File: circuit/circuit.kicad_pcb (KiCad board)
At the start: 2 copper layers, 19 parts

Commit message: circuit building
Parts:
- added BATT1: M02PTH, SparkFun:SparkFun-1X02_XTRA_BIG, F.Cu at (133.1, 81.8)
- added BATT2: M02PTH, SparkFun:SparkFun-1X02_XTRA_BIG, F.Cu at (133.1, 92.7)
- added BATT3: M02PTH, SparkFun:SparkFun-1X02_XTRA_BIG, F.Cu at (133.2, 103.3)
- added BATT4: M02PTH, SparkFun:SparkFun-1X02_XTRA_BIG, F.Cu at (133.2, 114.3)
- added C-ADC1: 100n, Capacitors_SMD:C_0805_HandSoldering, F.Cu at (140.4, 84.2)
- added CON-PV1: BARREL_JACK, Connect:JACK_ALIM, B.Cu at (165.8, 93.7)
- added C_VUSB1: 100u, Capacitors_ThroughHole:C_Radial_D5_L6_P2.5, B.Cu at (135.1, 135.2)
- added C_VUSB2: 100u, Capacitors_ThroughHole:C_Radial_D5_L6_P2.5, B.Cu at (135.1, 142.0)
- added D-3V3: D, Diodes_SMD:SMA_Handsoldering, F.Cu at (150.4, 95.5)
- added D-LAMP1: D, Diodes_SMD:SMA_Handsoldering, F.Cu at (172.0, 122.7)
- added D-PV1: D, Diodes_SMD:SMA_Handsoldering, F.Cu at (171.7, 108.1)
- added D-USB1: D, Diodes_SMD:SMA_Handsoldering, F.Cu at (146.9, 131.3)
- added D-VDD1: D, Diodes_SMD:SMA_Handsoldering, F.Cu at (138.9, 103.9)
- added D-VUSB1: D_Schottky, Diodes_SMD:SMA_Handsoldering, F.Cu at (135.9, 131.3)
- added D-VUSB2: D_Schottky, Diodes_SMD:SMA_Handsoldering, F.Cu at (129.3, 149.1)
- added D1: 5v1, Diodes_SMD:MELF_Handsoldering, F.Cu at (138.5, 149.1)
- added IC-VUSB1: LM2596S, TO_SOT_Packages_SMD:TO-263-5Lead, F.Cu at (147.6, 140.0)
- added L-VUSB1: INDUCTOR, Inductors:INDUCTOR_V, B.Cu at (141.2, 139.7)
- added OK-LAMP1: PC817, Housings_DIP:DIP-4_W7.62mm, B.Cu at (156.3, 124.0)
- added OK-PV1: PC817, Housings_DIP:DIP-4_W7.62mm, B.Cu at (155.9, 84.9)
- added OK-PV2: PC817, Housings_DIP:DIP-4_W7.62mm, B.Cu at (155.9, 110.4)
- added OK-USB1: PC817, Housings_DIP:DIP-4_W7.62mm, B.Cu at (146.3, 115.6)
- added P-VDD-3V3: CONN_01X02, Pin_Headers:Pin_Header_Straight_1x02, B.Cu at (140.7, 95.5)
- added P1: USB_A, Connect:USB_A, B.Cu at (140.5, 153.2)
- added R-ADC-BATT1: 470k, Resistors_ThroughHole:Resistor_Horizontal_RM10mm, B.Cu at (137.3, 84.2)
- added R-ADC-BATT2: 100k, Resistors_ThroughHole:Resistor_Horizontal_RM10mm, B.Cu at (140.4, 84.2)
- added R-LAMP1: 330, Resistors_SMD:R_0805_HandSoldering, F.Cu at (159.5, 123.7)
- added R-LAMP2: 4k7, Resistors_SMD:R_0805_HandSoldering, F.Cu at (165.4, 117.9)
- added R-PV1: 4k7, Resistors_SMD:R_0805_HandSoldering, F.Cu at (152.2, 89.0)
- added R-PV2: 100k, Resistors_SMD:R_0805_HandSoldering, F.Cu at (158.8, 88.3)
- added R-PV3: 330, Resistors_SMD:R_0805_HandSoldering, F.Cu at (159.7, 113.4)
- added R-PV4: 4k7, Resistors_SMD:R_0805_HandSoldering, F.Cu at (161.6, 103.8)
- added R-USB1: 330, Resistors_SMD:R_0805_HandSoldering, F.Cu at (148.2, 118.1)
- added R-USB2: 4k7, Resistors_SMD:R_0805_HandSoldering, F.Cu at (151.9, 122.8)
- added SW-PWR1: CONN_01X02, Pin_Headers:Pin_Header_Straight_1x02, B.Cu at (128.6, 118.4)
- added TR-LAMP1: IRF530_TO220BV, transistor-power:TO220BV, B.Cu at (165.4, 123.2)
- added TR-PV1: IRF9530_TO220BV, transistor-power:TO220BV, B.Cu at (164.7, 108.2)
- added TR-USB1: IRF530_TO220BV, transistor-power:TO220BV, B.Cu at (146.1, 124.5)
- added U1: MIC5219BM5_SOT23-5, TO_SOT_Packages_SMD:SOT-23-5, F.Cu at (145.1, 101.9)
- L-LAMP1, L-PV1, L-USB1, L1, L2, L3, L4: footprint LEDs:LED-1206 -> LEDs:LED-0805
- P-BOOT1, P-COMM1, SW-NRST1: moved to B.Cu
- R-L-LAMP1, R-L-PV1, R-L-USB1, R-L1, R-L2, R-L3, R-L4, R-NRST1: footprint Resistors_SMD:R_1206_HandSoldering -> Resistors_SMD:R_0805_HandSoldering
- moved STM32 31.7 mm to (152.6, 72.4)
- moved SW-NRST1 31.5 mm to (138.9, 68.2), turned to 90 degrees
- moved R-NRST1 31.0 mm to (143.7, 68.3)
- moved P-COMM1 30.9 mm to (167.8, 65.9), turned to 180 degrees
- moved R-L2 30.6 mm to (152.2, 57.7)
- moved R-L-PV1 30.6 mm to (163.0, 57.8)
- moved R-L4 30.6 mm to (157.7, 57.7)
- moved R-L-LAMP1 30.6 mm to (143.4, 57.3)
- moved R-L-USB1 30.6 mm to (140.7, 57.3)
- moved R-L1 30.6 mm to (149.4, 57.7)
- moved R-L3 30.6 mm to (155.0, 57.7)
- moved L1 29.2 mm to (149.3, 52.7)
- moved L-LAMP1 29.2 mm to (143.2, 52.5)
- moved L-PV1 29.2 mm to (162.6, 52.6)
- moved L-USB1 29.2 mm to (140.4, 52.5)
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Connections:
- P-COMM1 pad 3: /TX -> /RX
- P-COMM1 pad 4: /RX -> /TX
- STM32 pad 10: /ADC_PV_WKUP -> /IND_PV_WKUP
- STM32 pad 25: Net-(STM32-Pad25) -> /CON_PV
- STM32 pad 26: Net-(STM32-Pad26) -> /CON_LAMP
- STM32 pad 27: Net-(STM32-Pad27) -> /CON_USB
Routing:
- net GND: track 0.00 -> 39.6 mm
- net /ADC_BATT: track 0.00 -> 24.7 mm, vias 0 -> 2
- net /IND_PV_WKUP: track 0.00 -> 23.8 mm
- net /BOOT0: track 0.00 -> 23.3 mm
- net /L-USB: track 0.00 -> 16.0 mm
- net /L-PV: track 0.00 -> 15.5 mm
- net /L-LAMP: track 0.00 -> 14.0 mm
- net GNDPWR: track 0.00 -> 12.5 mm
- net /TX: track 0.00 -> 11.4 mm
- net /RX: track 0.00 -> 11.3 mm
- net /L-L4: track 0.00 -> 10.9 mm
- net /L-L1: track 0.00 -> 10.2 mm
- net /NRST: track 0.00 -> 9.08 mm
- net Net-(OK-PV2-Pad3): track 0.00 -> 9.07 mm
- net /L-L3: track 0.00 -> 9.05 mm
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
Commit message: development
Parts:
- added L-IND1: LED, LEDs:LED-0805, F.Cu at (166.6, 52.6)
- added R-L-IND1: 330, Resistors_SMD:R_0805_HandSoldering, F.Cu at (166.6, 57.6)
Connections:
- STM32 pad 38: Net-(STM32-Pad38) -> /L-IND
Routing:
- net /L-IND: track 0.00 -> 18.8 mm
- net GND: track 39.6 -> 43.6 mm
- net Net-(L-IND1-Pad2): track 0.00 -> 2.57 mm

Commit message: circuit building
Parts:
- added C-VREG1: C, Capacitors_SMD:C_0805_HandSoldering, F.Cu at (155.3, 89.0)
- added C-VREG2: C, Capacitors_SMD:C_0805_HandSoldering, F.Cu at (151.7, 87.9)
- added D-LAMP2: D, Diodes_SMD:SMA_Handsoldering, F.Cu at (185.2, 68.0)
- added D-LAMP3: D_Schottky, Diodes_SMD:SMA_Handsoldering, F.Cu at (208.5, 69.8)
- added J1: audio-jack, audio-lamp:JACK_LAPAN, B.Cu at (212.7, 56.3)
- added P2: CONN_01X04, Pin_Headers:Pin_Header_Straight_1x04, B.Cu at (108.1, 62.2)
- added PIN1: CONN_01X03, Pin_Headers:Pin_Header_Straight_1x03, B.Cu at (108.2, 93.4)
- added PIN2: CONN_01X06, Pin_Headers:Pin_Header_Straight_1x06, B.Cu at (128.0, 85.7)
- added PIN3: CONN_01X02, Pin_Headers:Pin_Header_Straight_1x02, B.Cu at (128.3, 62.4)
- moved P1 86.4 mm to (203.1, 93.7), turned to 270 degrees
- moved D-VUSB2 82.5 mm to (199.0, 104.9), turned to 0 degrees
- moved D1 80.8 mm to (199.0, 95.6), turned to 270 degrees
- moved L-IND1 73.2 mm to (95.4, 69.6), turned to 0 degrees
- moved C_VUSB2 71.2 mm to (191.9, 99.0), turned to 0 degrees
- moved P-BOOT1 71.1 mm to (91.2, 91.8), turned to 0 degrees
- moved L-PV1 70.4 mm to (95.4, 73.6), turned to 0 degrees
- moved IC-VUSB1 68.1 mm to (189.9, 86.6), turned to 90 degrees
- moved L4 67.4 mm to (95.4, 78.6), turned to 0 degrees
- moved R-L-IND1 67.4 mm to (100.3, 69.6), turned to 0 degrees
- moved L-VUSB1 67.3 mm to (189.6, 92.9), turned to 180 degrees
- moved L3 66.1 mm to (95.4, 81.4), turned to 0 degrees
- moved L2 64.8 mm to (95.4, 84.2), turned to 0 degrees
- moved R-L-PV1 64.3 mm to (100.5, 73.3), turned to 0 degrees
- moved L1 63.8 mm to (95.4, 87.0), turned to 0 degrees
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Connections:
- P-BOOT1 pad 1: /BOOT0 -> VDD
- P-BOOT1 pad 2: VDD -> /BOOT0
- STM32 pad 1: Net-(STM32-Pad1) -> VDD
- STM32 pad 14: Net-(STM32-Pad14) -> /AIN4
- STM32 pad 15: Net-(STM32-Pad15) -> /AIN5
- STM32 pad 16: Net-(STM32-Pad16) -> /AIN6
- STM32 pad 17: Net-(STM32-Pad17) -> /AIN7
- STM32 pad 18: Net-(STM32-Pad18) -> /AIN8
- STM32 pad 19: Net-(STM32-Pad19) -> /AIN9
- STM32 pad 2: Net-(STM32-Pad2) -> /PC13
- STM32 pad 28: Net-(STM32-Pad28) -> /PB15
- STM32 pad 29: Net-(STM32-Pad29) -> /PA8
- STM32 pad 3: Net-(STM32-Pad3) -> /PC14
- STM32 pad 32: Net-(STM32-Pad32) -> /PA11
- STM32 pad 33: Net-(STM32-Pad33) -> /PA12
- STM32 pad 34: Net-(STM32-Pad34) -> /PA13
- STM32 pad 37: Net-(STM32-Pad37) -> /PA14
- STM32 pad 4: Net-(STM32-Pad4) -> /PC15
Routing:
- net GND: track 43.6 -> 122.0 mm
- net +3V3: track 0.00 -> 39.3 mm
- net Net-(C_VUSB2-Pad1): track 0.00 -> 25.6 mm
- net /PA14: track 0.00 -> 25.1 mm
- net /PB15: track 0.00 -> 24.3 mm
- net /ADC_USB: track 0.00 -> 23.1 mm
- net /PA13: track 0.00 -> 22.9 mm
- net /PA8: track 0.00 -> 21.9 mm
- net /PA12: track 0.00 -> 21.4 mm
- net /PA11: track 0.00 -> 20.2 mm
- net +15V: track 4.30 -> 22.7 mm
- net /ADC_BATT: track 24.7 -> 6.94 mm, vias 2 -> 0
- net /AIN9: track 0.00 -> 16.4 mm
- net /AIN8: track 0.00 -> 14.8 mm
- net Net-(D-VUSB1-Pad1): track 0.00 -> 13.8 mm
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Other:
- board outline added: 128.8 x 53.9 mm

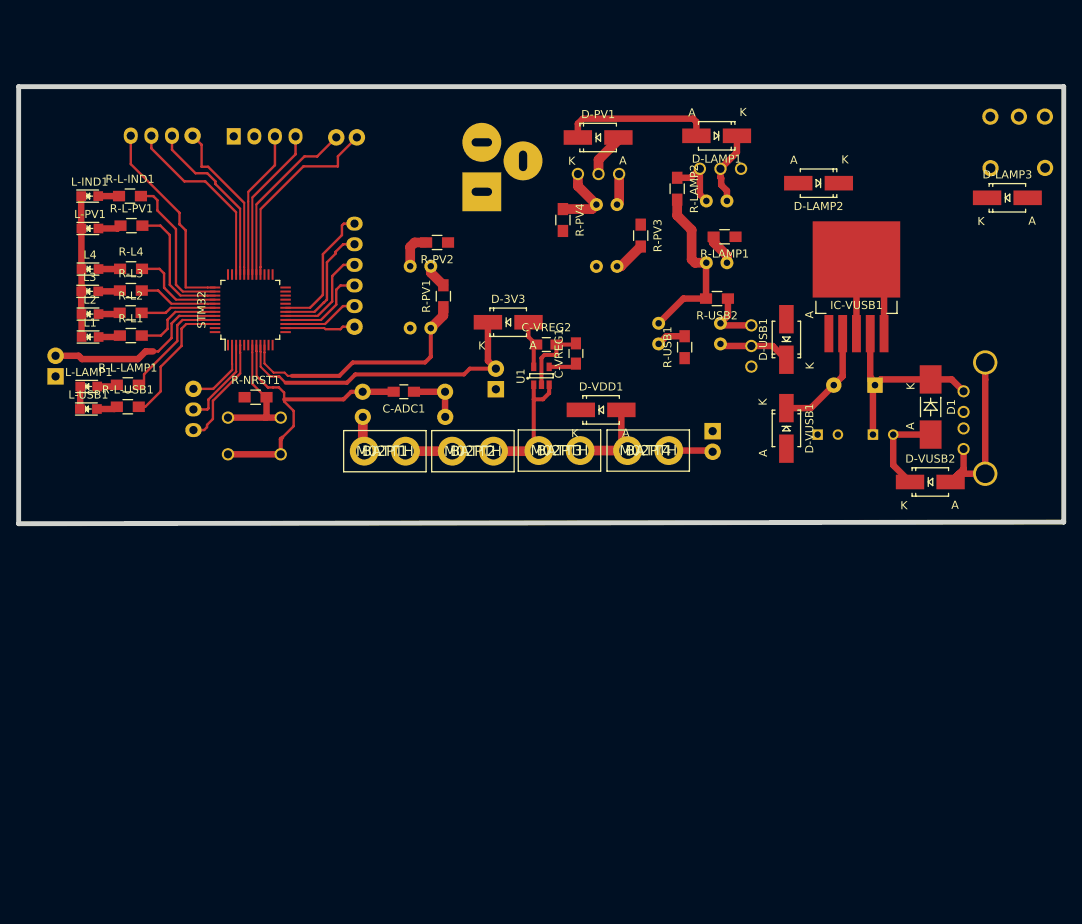
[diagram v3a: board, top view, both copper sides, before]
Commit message: tambah test pad
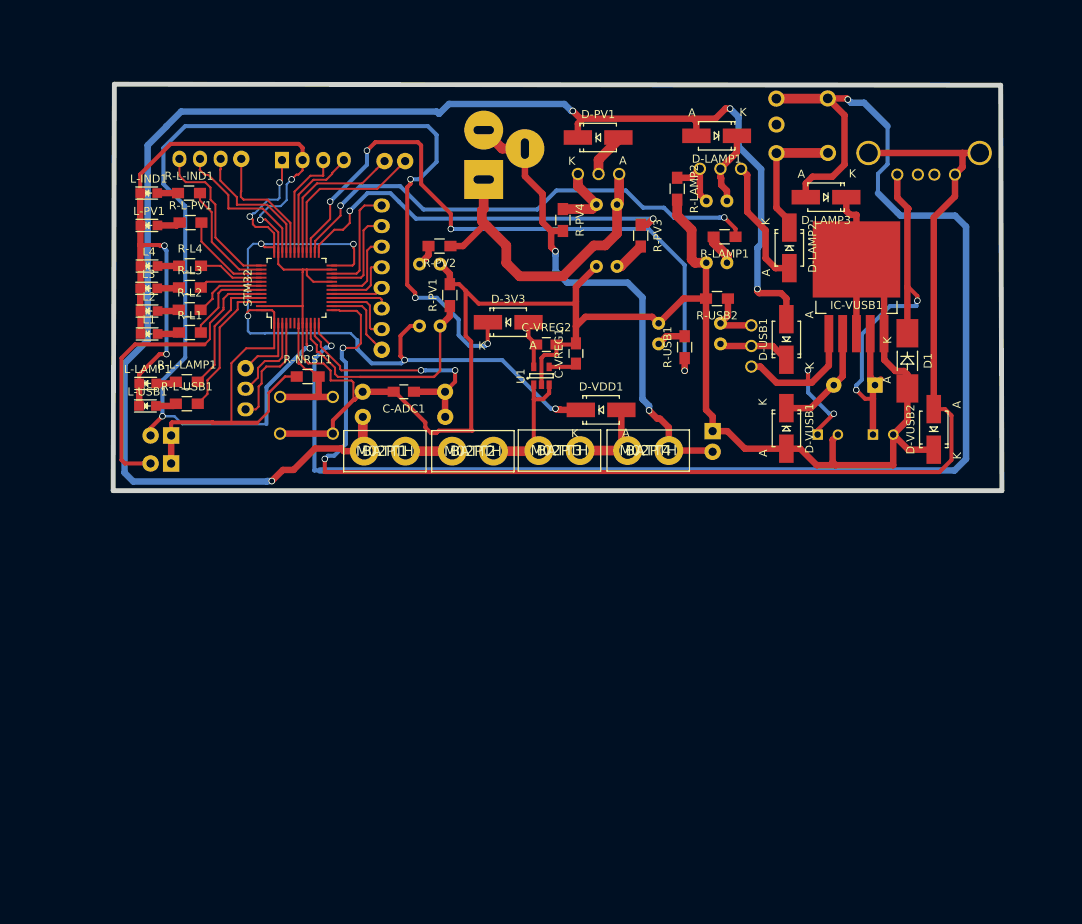
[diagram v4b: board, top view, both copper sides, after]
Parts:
- removed P2: CONN_01X04, Pin_Headers:Pin_Header_Straight_1x04
- added PIN4: CONN_01X04, Pin_Headers:Pin_Header_Straight_1x04, B.Cu at (114.1, 65.0)
- PIN2: value CONN_01X06 -> CONN_01X08; footprint Pin_Headers:Pin_Header_Straight_1x06 -> Pin_Headers:Pin_Header_Straight_1x08
- moved P-VDD-3V3 40.4 mm to (105.4, 99.1), turned to 90 degrees
- moved J1 36.2 mm to (176.5, 58.0), turned to 270 degrees
- moved P1 27.9 mm to (194.9, 67.0), turned to 0 degrees
- moved D-LAMP3 22.4 mm to (186.1, 69.8), turned to 180 degrees
- moved P-BOOT1 17.8 mm to (105.4, 102.6), turned to 90 degrees
- moved D-LAMP2 8.75 mm to (181.6, 76.0), turned to 270 degrees
- moved L-IND1 7.28 mm to (102.7, 69.2)
- moved L-LAMP1 7.28 mm to (102.5, 92.7)
- moved L-USB1 7.28 mm to (102.5, 95.5)
- moved L1 7.28 mm to (102.7, 86.6)
- moved L3 7.28 mm to (102.7, 81.0)
- moved R-L-PV1 7.28 mm to (107.8, 72.9)
- moved R-L2 7.28 mm to (107.7, 83.6)
- moved R-L4 7.28 mm to (107.8, 78.2)
- moved L-PV1 7.28 mm to (102.7, 73.2)
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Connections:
- STM32 pad 21: Net-(STM32-Pad21) -> /PB10
- STM32 pad 22: Net-(STM32-Pad22) -> /PB11
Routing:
- net GND: track 122.0 -> 338.9 mm, vias 0 -> 4
- net /ADC_LAMP: track 0.00 -> 182.4 mm, vias 0 -> 2
- net +15V: track 22.7 -> 188.7 mm, vias 0 -> 4
- net VDD: track 0.00 -> 146.0 mm, vias 0 -> 7
- net /ADC_USB: track 23.1 -> 159.5 mm, vias 0 -> 2
- net +3V3: track 39.3 -> 139.9 mm, vias 0 -> 5
- net /CON_USB: track 0.00 -> 79.8 mm, vias 0 -> 4
- net /CON_LAMP: track 0.00 -> 61.9 mm, vias 0 -> 2
- net GNDPWR: track 5.46 -> 62.1 mm, vias 0 -> 2
- net /CON_PV: track 0.00 -> 48.8 mm, vias 0 -> 2
- net +24V: track 3.88 -> 41.1 mm
- net Net-(C_VUSB2-Pad1): track 25.6 -> 55.8 mm, vias 0 -> 2
- net Net-(C_VUSB1-Pad1): track 0.00 -> 27.2 mm, vias 0 -> 2
- net /ADC_BATT: track 6.94 -> 31.3 mm, vias 0 -> 2
- net Net-(D-LAMP2-Pad1): track 0.00 -> 16.2 mm
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- added copper zone on B.Cu, net (none)
- added copper zone on F.Cu, net (none)
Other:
- board size 128.8 x 53.9 mm -> 109.5 x 50.1 mm
